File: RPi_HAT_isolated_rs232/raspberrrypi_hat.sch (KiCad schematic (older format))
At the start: 70 parts, among them J1 Conn_01x06, J21 Conn_01x02, J22 Conn_01x05, J3 40HAT, J40 Conn_02x03_Odd_Even, J9 CONN_01X02, Q1 Q_PNP_BEC, Q39 Q_PNP_BEC, U2 CAT24C32, U21 DC-DC_CUI_PDQE20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

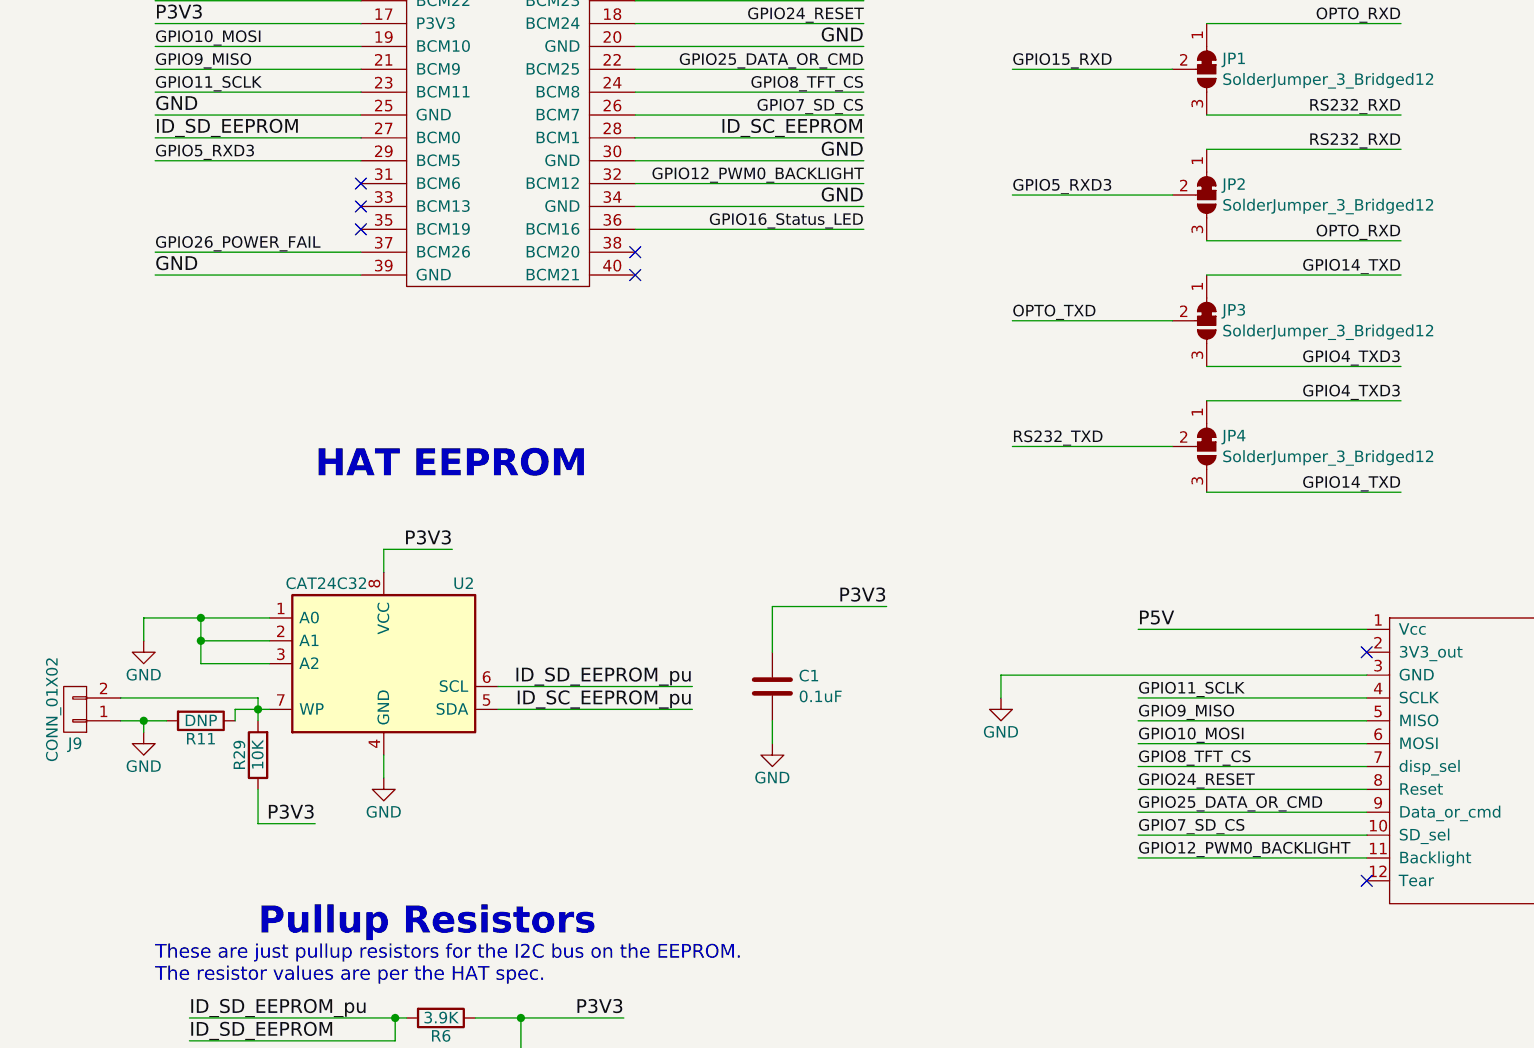
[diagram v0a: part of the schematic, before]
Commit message: This version was tested and something failed, see SuperCapUps7_rs232/bom.txt for details
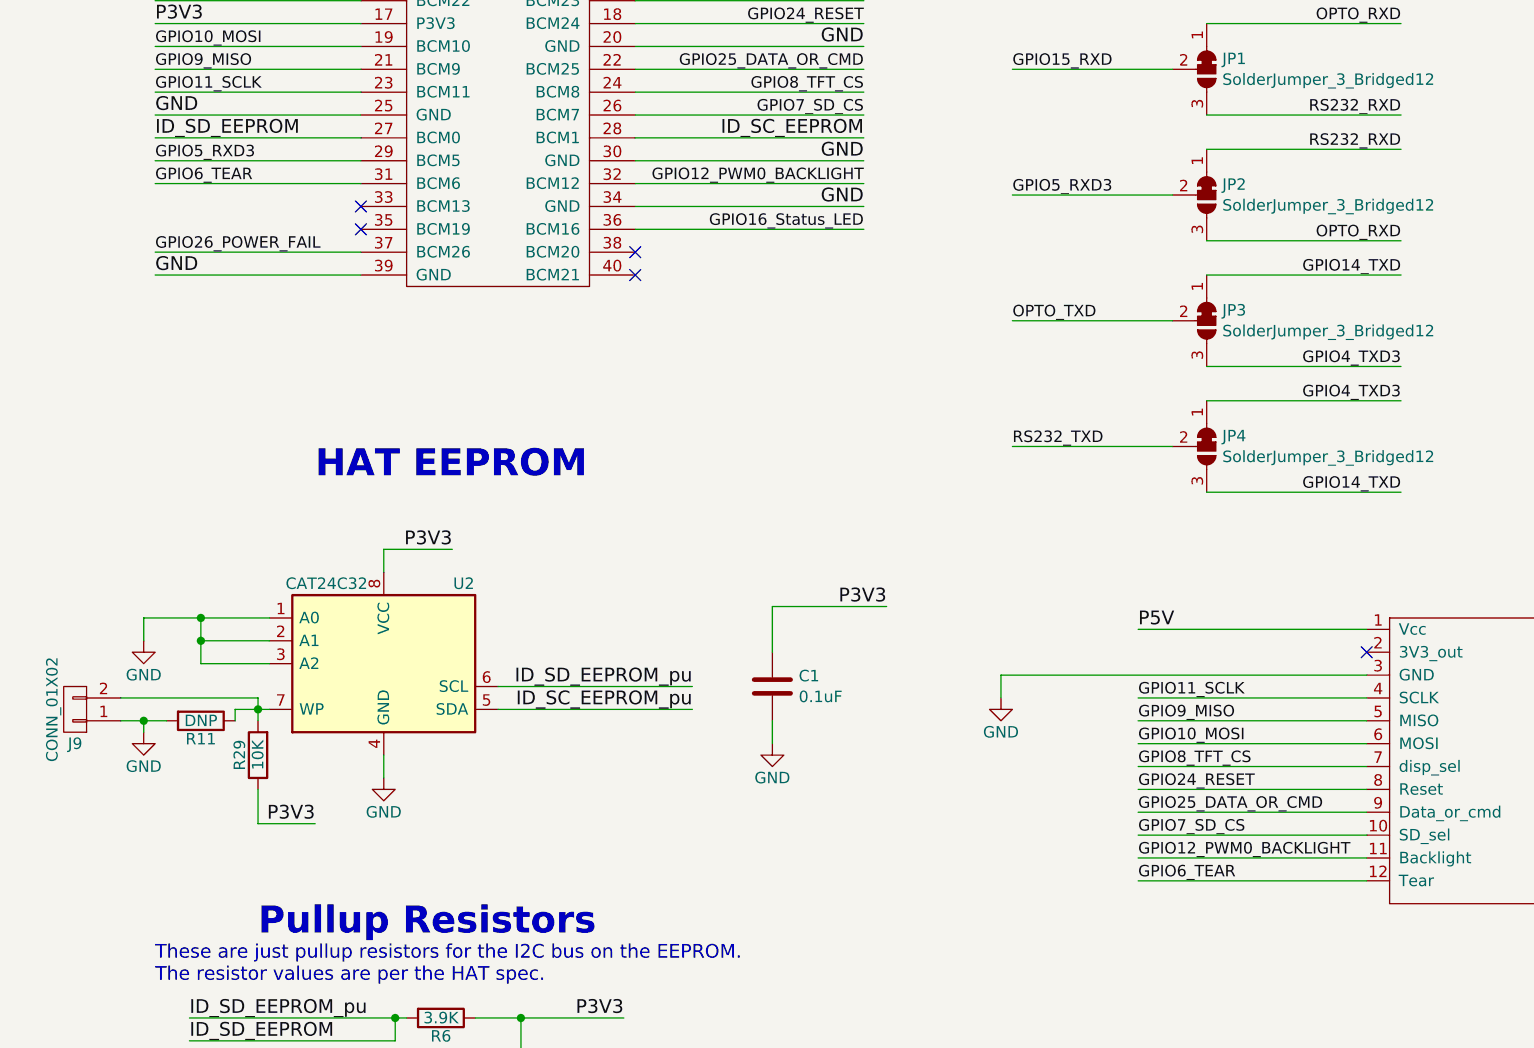
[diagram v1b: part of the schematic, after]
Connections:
- net GPIO6_TEAR: now reaches J3.31 (BCM6)
- net GPIO6_TEAR: now also U50.12 (Tear)
- no-connect marks 12 -> 10
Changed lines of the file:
@@
 Sheet 1 1
 Title "Raspberry Pi HAT"
-Date "2021-06-12"
+Date "2021-10-03"
 Rev "A"
 Comp ""
@@
 Text Label 5400 6300 0    50   ~ 0
 GPIO8_TFT_CS
-NoConn ~ 6400 6800
 Wire Wire Line
 	2000 4050 1100 4050
@@
 Wire Wire Line
 	1800 10750 2900 10750
-NoConn ~ 2000 3750
 Wire Wire Line
 	3200 3350 4200 3350
@@
 Wire Wire Line
 	1250 9700 1800 9700
+Wire Wire Line
+	2000 3750 1100 3750
+Text Label 1100 3750 0    50   ~ 0
+GPIO6_TEAR
+Wire Wire Line
+	6400 6800 5400 6800
+Text Label 5400 6800 0    50   ~ 0
+GPIO6_TEAR
 $EndSCHEMATC
